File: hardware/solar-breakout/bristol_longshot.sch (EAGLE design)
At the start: 65 parts, among them U1 SPV1040, U2 SPV1040, U3 LT4054ES5-4.2, U4 TPS62243, U5 TPS62243, U6 TPS3808, U7 74LVC1G04GW

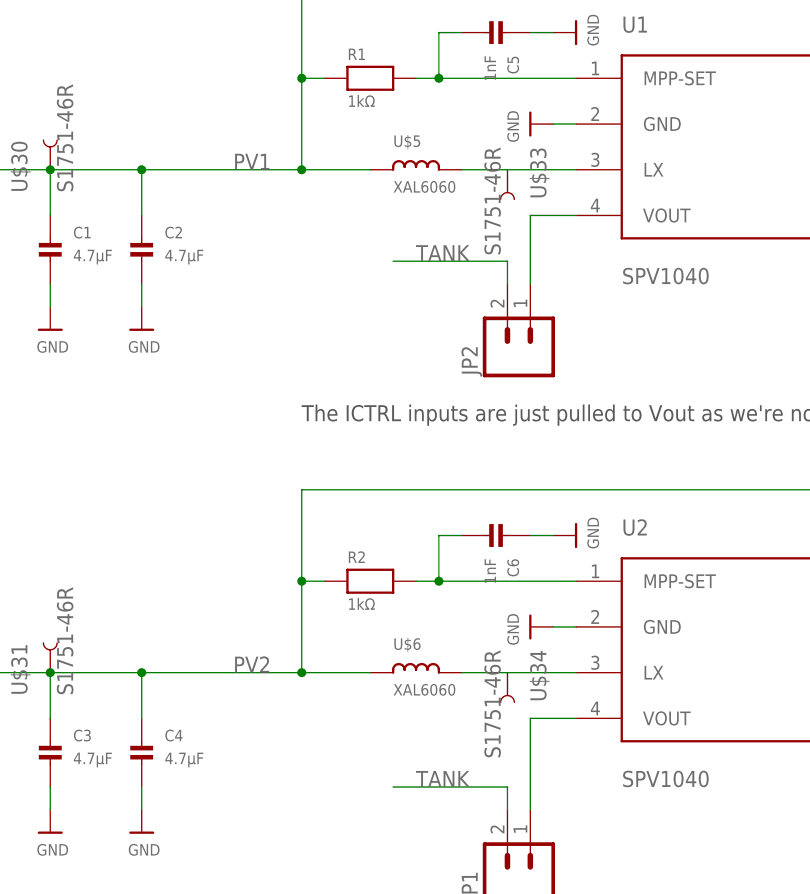
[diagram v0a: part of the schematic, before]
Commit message: Added LPS3015 mppt inductor footprint alongside XAL6060 footprint
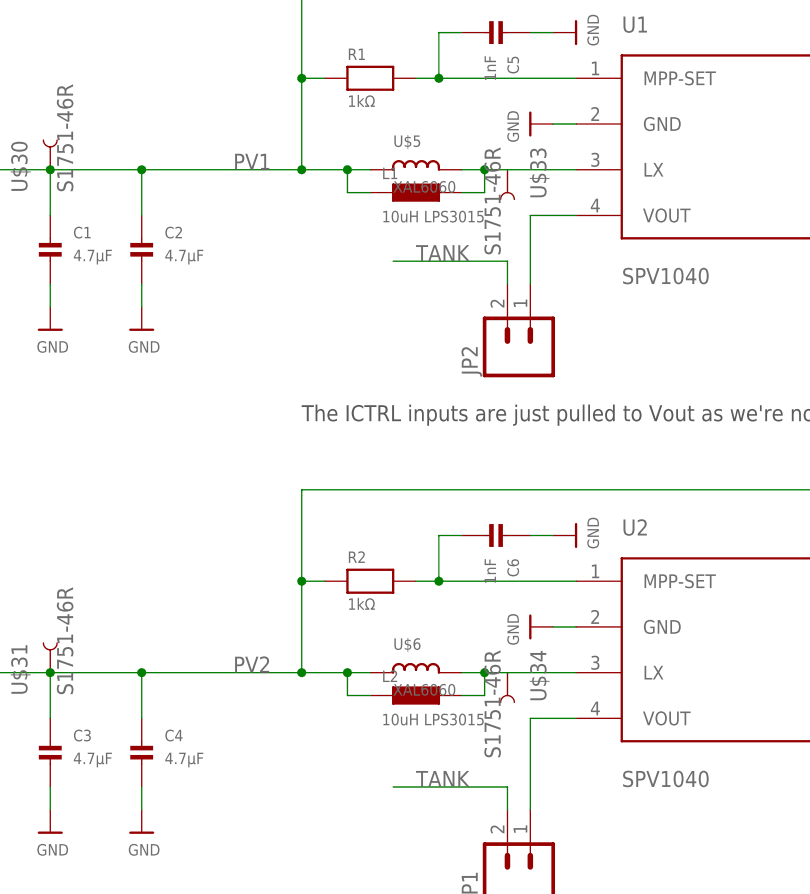
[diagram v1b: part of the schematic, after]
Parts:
- added L1, L2: 10uH LPS3015, PecanFemto4:IND-LPS3015
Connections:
- net LX1: now also L1.2
- net LX2: now also L2.2
- net PV1: now also L1.1
- net PV2: now also L2.1
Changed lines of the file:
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@@
 <?xml version="1.0" encoding="utf-8"?>
 <!DOCTYPE eagle SYSTEM "eagle.dtd">
-<eagle version="6.5.0">
+<eagle version="7.3.0">
 <drawing>
 <settings>
@@
 <layer number="54" name="bGND_GNDA" color="1" fill="9" visible="no" active="no"/>
 <layer number="56" name="wert" color="7" fill="1" visible="no" active="no"/>
+<layer number="57" name="tCAD" color="7" fill="1" visible="no" active="no"/>
 <layer number="91" name="Nets" color="2" fill="1" visible="yes" active="yes"/>
 <layer number="92" name="Busses" color="1" fill="1" visible="yes" active="yes"/>
@@
 <layer number="97" name="Info" color="7" fill="1" visible="yes" active="yes"/>
 <layer number="98" name="Guide" color="6" fill="1" visible="yes" active="yes"/>
+<layer number="99" name="SpiceOrder" color="7" fill="1" visible="yes" active="yes"/>
 <layer number="100" name="Muster" color="7" fill="1" visible="no" active="no"/>
 <layer number="101" name="Patch_Top" color="12" fill="4" visible="yes" active="yes"/>
@@
 <layer number="111" name="LPC17xx" color="7" fill="1" visible="yes" active="yes"/>
 <layer number="112" name="tSilk" color="7" fill="1" visible="yes" active="yes"/>
+<layer number="113" name="IDFDebug" color="4" fill="1" visible="yes" active="yes"/>
 <layer number="116" name="Patch_BOT" color="9" fill="4" visible="yes" active="yes"/>
 <layer number="121" name="_tsilk" color="7" fill="1" visible="yes" active="yes"/>
@@
 <layer number="132" name="bAdjust" color="7" fill="1" visible="no" active="yes"/>
 <layer number="144" name="Drill_legend" color="7" fill="1" visible="yes" active="yes"/>
+<layer number="150" name="Notes" color="7" fill="1" visible="yes" active="yes"/>
 <layer number="151" name="HeatSink" color="7" fill="1" visible="yes" active="yes"/>
 <layer number="152" name="_bDocu" color="7" fill="1" visible="yes" active="yes"/>
+<layer number="153" name="FabDoc1" color="7" fill="1" visible="yes" active="yes"/>
+<layer number="154" name="FabDoc2" color="7" fill="1" visible="yes" active="yes"/>
+<layer number="155" name="FabDoc3" color="7" fill="1" visible="yes" active="yes"/>
 <layer number="199" name="Contour" color="7" fill="1" visible="yes" active="yes"/>
 <layer number="200" name="200bmp" color="1" fill="10" visible="no" active="no"/>
@@
 <part name="C19" library="resistor" deviceset="C-EU" device="C0603K" value="10µF"/>
 <part name="U$26" library="microbuilder_v3" deviceset="GND" device=""/>
+<part name="L1" library="PecanFemto4" deviceset="IND-LPS3015" device="" value="10uH LPS3015"/>
+<part name="L2" library="PecanFemto4" deviceset="IND-LPS3015" device="" value="10uH LPS3015"/>
 </parts>
 <sheets>
@@
 <instance part="C19" gate="G$1" x="739.14" y="88.9"/>
 <instance part="U$26" gate="G$1" x="739.14" y="78.74"/>
+<instance part="L1" gate="G$1" x="81.28" y="121.92"/>
+<instance part="L2" gate="G$1" x="81.28" y="66.04"/>
 </instances>
 <busses>
@@
 <pinref part="U$33" gate="G$1" pin="1"/>
 <pinref part="U$5" gate="G$1" pin="2"/>
-<wire x1="91.44" y1="124.46" x2="86.36" y2="124.46" width="0.1524" layer="91"/>
+<wire x1="91.44" y1="124.46" x2="88.9" y2="124.46" width="0.1524" layer="91"/>
+<pinref part="L1" gate="G$1" pin="2"/>
+<wire x1="88.9" y1="124.46" x2="86.36" y2="124.46" width="0.1524" layer="91"/>
+<wire x1="86.36" y1="121.92" x2="88.9" y2="121.92" width="0.1524" layer="91"/>
+<wire x1="88.9" y1="121.92" x2="88.9" y2="124.46" width="0.1524" layer="91"/>
+<junction x="88.9" y="124.46"/>
 </segment>
 </net>
@@
 <pinref part="U$34" gate="G$1" pin="1"/>
 <pinref part="U$6" gate="G$1" pin="2"/>
-<wire x1="91.44" y1="68.58" x2="86.36" y2="68.58" width="0.1524" layer="91"/>
+<wire x1="91.44" y1="68.58" x2="88.9" y2="68.58" width="0.1524" layer="91"/>
+<pinref part="L2" gate="G$1" pin="2"/>
+<wire x1="88.9" y1="68.58" x2="86.36" y2="68.58" width="0.1524" layer="91"/>
+<wire x1="86.36" y1="66.04" x2="88.9" y2="66.04" width="0.1524" layer="91"/>
+<wire x1="88.9" y1="66.04" x2="88.9" y2="68.58" width="0.1524" layer="91"/>
+<junction x="88.9" y="68.58"/>
 </segment>
 </net>
 <net name="PV1" class="0">
 <segment>
-<wire x1="76.2" y1="124.46" x2="68.58" y2="124.46" width="0.1524" layer="91"/>
+<wire x1="76.2" y1="124.46" x2="73.66" y2="124.46" width="0.1524" layer="91"/>
 <label x="60.96" y="124.46" size="1.778" layer="95"/>
 <pinref part="R1" gate="G$1" pin="1"/>
+<wire x1="73.66" y1="124.46" x2="68.58" y2="124.46" width="0.1524" layer="91"/>
 <wire x1="68.58" y1="124.46" x2="50.8" y2="124.46" width="0.1524" layer="91"/>
 <wire x1="50.8" y1="124.46" x2="40.64" y2="124.46" width="0.1524" layer="91"/>
@@
 <pinref part="U$30" gate="G$1" pin="1"/>
 <pinref part="U$5" gate="G$1" pin="1"/>
+<pinref part="L1" gate="G$1" pin="1"/>
+<wire x1="76.2" y1="121.92" x2="73.66" y2="121.92" width="0.1524" layer="91"/>
+<wire x1="73.66" y1="121.92" x2="73.66" y2="124.46" width="0.1524" layer="91"/>
+<junction x="73.66" y="124.46"/>
 </segment>
 </net>
@@
 <pinref part="U$31" gate="G$1" pin="1"/>
 <pinref part="U$6" gate="G$1" pin="1"/>
-<wire x1="68.58" y1="68.58" x2="76.2" y2="68.58" width="0.1524" layer="91"/>
-</segment>
-</net>
+<wire x1="68.58" y1="68.58" x2="73.66" y2="68.58" width="0.1524" layer="91"/>
+<pinref part="L2" gate="G$1" pin="1"/>
+<wire x1="73.66" y1="68.58" x2="76.2" y2="68.58" width="0.1524" layer="91"/>
+<wire x1="76.2" y1="66.04" x2="73.66" y2="66.04" width="0.1524" layer="91"/>
+<wire x1="73.66" y1="66.04" x2="73.66" y2="68.58" width="0.1524" layer="91"/>
+<junction x="73.66" y="68.58"/>
+</segment>
+</net>

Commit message: Update solar breakout to yet another design
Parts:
- removed C10, C6, C8: 1nF, microbuilder_v3:CAP_CERAMIC_0402
- removed C12, C13, C14, C16, C4: 4.7µF, microbuilder_v3:CAP_CERAMIC_0402
- removed C17, C18, C19: 10µF, resistor:C-EUC0603K
- removed D4: BAT760, BAT760:BAT760
- removed D6: DIODE[TVS], nxp:DIODE[TVS]
- removed L2: 10uH LPS3015, PecanFemto4:IND-LPS3015
- removed L4: 2.2µH, SparkFun:INDUCTOR1007
- removed R2: 1kΩ, microbuilder_v3:RESISTOR_0402
- removed R3, R4: 10kΩ, microbuilder_v3:RESISTOR_0402
- removed R6: 220kΩ, microbuilder_v3:RESISTOR_0402
- removed R8: 82kΩ, microbuilder_v3:RESISTOR_0402
- removed R9: 2.2kΩ, microbuilder_v3:RESISTOR_0402
- removed U$25, U$30, U$31, U$33, U$34, U$39, U$41, U$42, U$43, U$44, U$45, U$46, U$47: S1751-46R, Harwin-Test-Point:S1751-46R
- removed U$5, U$6: XAL6060, XAL6060:XAL6060
- removed U3: LT4054ES5-4.2, XYKlib:LT4054ES5-4.2
- removed U5: TPS62243, TPS62243:TPS62243
- removed U6: TPS3808, TPS3808:TPS3808
- removed U7: 74LVC1G04GW, 74LVC1G04GW_inverter:74LVC1G04GW
- added C30: 10µF, resistor:C-EUC0603K
- added C32: 100µF, resistor:C-EUC1206K
- added JP10, JP12, JP13, JP14, JP8, JP9: (no value), SparkFun:M02LOCK
- added JP11: (no value), SparkFun:M023.5MM_LOCK
- added Q2, Q3: BSS84, nxp:NX2301P
- added R15: 1MΩ, microbuilder_v3:RESISTOR_0402
- C1, C2, C3: value 4.7µF -> 10µF; device microbuilder_v3:CAP_CERAMIC_0402 -> resistor:C-EUC0603K
- D3: value BAT760 -> RB161M; device BAT760:BAT760 -> RB161M:RB161M
- JP4: value PV2 -> (none); device SparkFun:M023.5MM_LOCK -> SparkFun:M02LOCK
- JP6: value Shutdown -> (none)
- JP7: device SparkFun:M04LOCK -> SparkFun:M02LOCK
- U2: value SPV1040 -> LTC4071EMS8EPBF; device spv1040:SPV1040 -> LTC4071_EMS8:LTC4071EMS8EPBF
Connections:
- removed net BATTERY_BUCK_SW: L4.1, U$46.1, U5.SW
- removed net BATTERY_EN: R3.1, U$44.1, U5.EN, U7.Y
- removed net CHG: D2.C, U3.CHRG
- removed net CT: U6.CT
- removed net LX1: L1.2, U$33.1, U$5.2, U1.LX
- removed net LX2: L2.2, U$34.1, U$6.2, U2.LX
- removed net MPP-SET2: C6.P$2, R2.2, U2.MPP-SET
- removed net MPPT-VOUT-1: C13.P$1, D5.2, JP2.1, R5.2, U1.ICTRL+, U1.ICTRL-, U1.VOUT
- removed net MPPT-VOUT-2: C14.P$1, D6.2, JP1.1, R6.2, U2.ICTRL+, U2.ICTRL-, U2.VOUT
- removed net N$1: C5.P$2, R1.2, U1.MPP-SET
- removed net N$5: JP6.1, R9.1
- removed net PROG: R9.2, U$25.1, U3.PROG
- removed net PV1: C1.P$1, C2.P$1, JP3.1, L1.1, R1.1, U$30.1, U$5.1, U1.XSHUT
- removed net PV2: C3.P$1, C4.P$1, JP4.1, L2.1, R2.1, U$31.1, U$6.1, U2.XSHUT
- removed net SPV_VCTRL1: C7.P$1, R5.1, R7.2, U1.VCTRL
- removed net SPV_VCTRL2: C8.P$1, R6.1, R8.2, U2.VCTRL
- removed net SUPERVISOR_VCC: C10.P$1, D3.C, D4.C, R3.2, R4.2, U$47.1, U6.VDD, U7.VCC
- removed net TANK: C11.P$1, C15.P$1, D4.A, JP1.2, JP2.2, R10.2, U$41.1, U3.VCC, U4.VIN, U6.SENSE
- removed net TANK_BUCK_SW: L3.1, U$45.1, U4.SW
- removed net TANK_EN: R4.1, U$43.1, U4.EN, U6.!RESET, U7.A
- new net BATTERY_MOSFET_1: Q2.D, Q3.S
- new net BATTERY_VCC: C11.P$1, D3.A, JP12.1, Q3.D, U2.NTC, U2.VCC
- new net BATT_MOSFET_CTRL: JP6.1, Q2.G, Q3.G, R15.2
- new net HBO: R10.2, U2.HBO
- new net LX: JP8.1, L1.2, U1.LX
- new net MPPT_VOUT: C2.1, C32.1, D5.2, JP2.1, JP7.1, R5.2, U1.ICTRL+, U1.ICTRL-, U1.VOUT
- new net MPP_SET: C5.P$2, JP4.1, R1.2, U1.MPP-SET
- new net N$7: L3.1, U4.SW
- new net PV: C1.1, JP1.1, JP3.1, L1.1, R1.1, U1.XSHUT
- new net SOLAR: C15.P$1, D3.C, JP14.1, JP2.2, Q2.S, R15.1, U4.EN, U4.VIN
- new net SPV_VCTRL: C7.P$1, JP9.1, R5.1, R7.2, U1.VCTRL
- net 1.8V: now also C3.1, JP10.1, JP11.1; no longer C17.1, C18.1, C19.1, L4.2, U$42.1, U5.FB
- net BATTERY: now also C30.1, JP13.1, U2.BAT; no longer C12.P$1, C16.P$1, D3.A, U$39.1, U3.BAT, U5.VIN
- net GND: now also C1.2, C2.2, C3.2, C30.2, C32.2, D2.C, JP1.2, JP10.2, JP11.2, JP12.2, JP13.2, JP14.2, JP8.2, JP9.2, U2.ADJ, U2.EP, U2.LBSEL; no longer C1.P$2, C10.P$2, C12.P$2, C13.P$2, C14.P$2, C16.P$2, C17.2, C18.2, C19.2, C2.P$2, C3.P$2, C4.P$2, C6.P$1, C8.P$2, D6.1, JP7.1, JP7.3, JP7.4, R8.1, U3.GND, U5.GND, U5.GND2, U5.MODE, U6.GND, U6.GND2, U7.GND
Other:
- note added: "Battery is cutoff when < 3.2V. LTC4071 shunts current when battery > 4.0V."
- note added: "Connect to enable battery charging"
- note added: "Could use the body diode of the MOSFETs but Vf is lower this way"
- note added: "For V_gs = -4V, Id_max = 200mA R_DSon = 10Ω"
- note added: "Input voltage 2v - 2.4v from 4x solar panel"
- note added: "MOSFET operates in resistive region during normal operation. If solar voltage drops the MOSFETs cutoff battery charging first."
- note added: "Max. voltage from solar is 4.6V"
- note added: "NTC not used Float Voltage = 4.0V Low Batt. Cutoff = 3.2V"
- note added: "Start of cycle: Vd = 4.6-3.2V = 1.4V I = 70mA End of cycle: Vd = 4.6V-4V = 0.6V, I = 30mA"
- note added: "Vout set = 4.6V"
- note added: "We draw power from both Solar and Battery"
- note removed: "!MR! has internal pull-up"
- note removed: "Ichg = 150V / Rchg"
- note removed: "Ichg can be measured by Vprog"
- note removed: "Leaving Ct open sets the reset time (transition battery->solar) to 20ms"
- note removed: "Rchg = 2.2kΩ gives Ichg = 70mA"
- note removed: "Still quite unsure on inductor value.. but 2.2µH is worth trying, since it would be much better than the recommended 10µH. Will the boost then run in inefficient discontinous mode????"
- note removed: "The 2nd MPPT can be connected to Vtank with a jumper"
- moved on the sheet: C1, C11, C15, C2, C3, C5, C7, D2, D5, JP1, JP2, JP3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

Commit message: [solar-breakout] Complete parts list
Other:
- note added: "Current idea: Omit LTC4071 entirely. Requirement for 2.1V to drive diode+reg prevents v. deep discharge. This will be rare anyhow and should only occour in the polar night. Limit SPV1040 to 4.4V instead. 60mA @ 3.2V, 10mA @ 4.2V How to limit charging during to first half hour while battery is still cold? Has to get to -10ºC to enable charging? (hysterisis at -20ºC?) Needs an IO line... Replace LE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"
- note added: "EDIT: Low Batt Cuttoff = 2.7V on low-power-solar"
- note added: "EDIT: Not sure if standard cutoffs are useful. The internal resistance is too large. Discharge: Current pulses cutoff battery when plenty of charge remains. Other shutdown mechanism that operates only in quiescent state? Vsolar < Vcutt for 30s+?? Timer based on expected capacity? Just measure Vsolar before drawing significant current. Charge: Internal resistance increases charging voltage. TODO: 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"
- note added: "R5 = 220kΩ, R7 = 82kΩ Vout set = 4.6V R5 = 180kΩ, R7 = 71.5kΩ Vout set = 4.4V"
- note added: "Replace LTC4071 with a 4.3V zener diode. Or replace with LTC4070 with float voltage = 4.1V. Pin 7 would be n/c Bump up SPV output voltage to 4.7V nom (4.8V max) for 20mA termination current."
- note removed: "Vout set = 4.6V"
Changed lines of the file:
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@@
 from 4x solar panel</text>
 <text x="558.8" y="139.7" size="1.778" layer="97">We draw power from both Solar and Battery</text>
-<text x="157.48" y="73.66" size="1.778" layer="97">Vout set = 4.6V</text>
+<text x="157.48" y="63.5" size="1.778" layer="97">R5 = 220kΩ, R7 = 82kΩ
+Vout set = 4.6V
+R5 = 180kΩ, R7 = 71.5kΩ
+Vout set = 4.4V</text>
 <text x="20.32" y="71.12" size="1.778" layer="97">&gt;2V is enough
 to self-start conversion</text>
@@
 <text x="558.8" y="129.54" size="1.778" layer="97">Could use the body diode of the MOSFETs
 but Vf is lower this way</text>
+<text x="261.62" y="195.58" size="2.54" layer="97">EDIT: Not sure if standard cutoffs are useful. The internal resistance is too large.
+Discharge: Current pulses cutoff battery when plenty of charge remains.
+Other shutdown mechanism that operates only in quiescent state?
+Vsolar &lt; Vcutt for 30s+?? Timer based on expected capacity? Just measure Vsolar before drawing significant current.
+Charge: Internal resistance increases charging voltage. TODO: Measure IR at 0ºC/-10ºC.
+Batt gets to -10ºC in the sun most days.</text>
+<text x="370.84" y="55.88" size="2.54" layer="97">EDIT: Low Batt Cuttoff
+= 2.7V on low-power-solar</text>
+<text x="261.62" y="157.48" size="2.54" layer="97">Current idea: Omit LTC4071 entirely. Requirement for 2.1V to drive diode+reg
+prevents v. deep discharge. This will be rare anyhow and should only occour
+in the polar night.
+Limit SPV1040 to 4.4V instead. 60mA @ 3.2V, 10mA @ 4.2V
+How to limit charging during to first half hour while battery is still cold? Has to get to -10ºC to enable charging? (hysterisis at -20ºC?)
+Needs an IO line... Replace LED? Needs an npn transistor to pull low</text>
+<text x="266.7" y="40.64" size="2.54" layer="97">Replace LTC4071 with a 4.3V zener diode.
+Or replace with LTC4070 with float voltage = 4.1V. Pin 7 would be n/c
+Bump up SPV output voltage to 4.7V nom (4.8V max) for 20mA termination current.</text>
 </plain>
 <instances>

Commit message: [solar-breakout] replace LTC4071 -> LTC4070 as tested
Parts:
- removed C11: 4.7µF, microbuilder_v3:CAP_CERAMIC_0402
- removed C30: 10µF, resistor:C-EUC0603K
- removed Q3: BSS84, nxp:NX2301P
- removed R10: 330Ω, microbuilder_v3:RESISTOR_0402
- added C6, C8: 10µF, resistor:C-EUC0603K
- added Q1: BSS84, nxp:NX2301P
- added R2: 220kΩ, microbuilder_v3:RESISTOR_0402
- C1, C2: value 10µF -> 1nF; device resistor:C-EUC0603K -> microbuilder_v3:CAP_CERAMIC_0402
- C3: value 10µF -> 1µF; device resistor:C-EUC0603K -> microbuilder_v3:CAP_CERAMIC_0402
- C5, C7: value 1nF -> 10µF; device microbuilder_v3:CAP_CERAMIC_0402 -> resistor:C-EUC0603K
- D2: value GREEN -> RB161M; device led:LEDCHIPLED_0603 -> RB161M:RB161M
- D3: value RB161M -> GREEN; device RB161M:RB161M -> led:LEDCHIPLED_0603
- R5: value 220kΩ -> 330Ω
- U2: value LTC4071EMS8EPBF -> LTC4070EMS8EPBF; device LTC4071_EMS8:LTC4071EMS8EPBF -> LTC4070_EMS8:LTC4070EMS8EPBF
- renumbered C15 to C4, C32 to C9, D5 to D1, L3 to L2, R15 to R4, R7 to R3, U4 to U3
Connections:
- removed net BATTERY_VCC: C11.P$1, D3.A, JP12.1, Q3.D, U2.NTC, U2.VCC
- net 1.8V: now also C8.1; no longer C3.1
- net BATTERY: now also C3.P$1, C7.1, D2.A, JP12.1, Q2.D, U2.NTC, U2.VCC; no longer C30.1, U2.BAT
- net BATTERY_MOSFET_1: now also Q1.D, Q2.S; no longer Q2.D, Q3.S
- net BATT_MOSFET_CTRL: now also Q1.G; no longer Q3.G
- net CHG_LED: now also D3.A, R5.1; no longer D2.A, R10.1
- net GND: now also C1.P$1, C2.P$2, C3.P$2, C5.2, C6.2, C7.2, C8.2, D3.C; no longer C1.2, C11.P$2, C2.2, C3.2, C30.2, C5.P$1, C7.P$2, D2.C, U2.LBSEL
- net HBO: now also R5.2; no longer R10.2
- net MPPT_VOUT: now also C6.1, R2.2; no longer C2.1, R5.2
- net MPP_SET: now also C1.P$2; no longer C5.P$2
- net PV: now also C5.1; no longer C1.1
- net SOLAR: now also D2.C, Q1.S; no longer D3.C, Q2.S
- net SPV_VCTRL: now also C2.P$1, R2.1; no longer C7.P$1, R5.1
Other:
- note added: "LTC4071 shunts current when battery > 4.0V."
- note added: "NTC not used ADJ = GND -> Float Voltage = 4.0V"
- note added: "R2 = 220kΩ, R3 = 82kΩ Vout set = 4.6V R2 = 180kΩ, R3 = 71.5kΩ Vout set = 4.4V"
- note removed: "Battery is cutoff when < 3.2V. LTC4071 shunts current when battery > 4.0V."
- note removed: "NTC not used Float Voltage = 4.0V Low Batt. Cutoff = 3.2V"
- note removed: "R5 = 220kΩ, R7 = 82kΩ Vout set = 4.6V R5 = 180kΩ, R7 = 71.5kΩ Vout set = 4.4V"
- moved on the sheet: C1, C2, C3, C5, C7, Q2, R5, U2
